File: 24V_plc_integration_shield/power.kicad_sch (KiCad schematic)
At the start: 9 parts, among them J2 USB_A_Stacked, J4 Screw_Terminal_01x02, J5 Conn_01x02_Female, U4 JTD2024S05

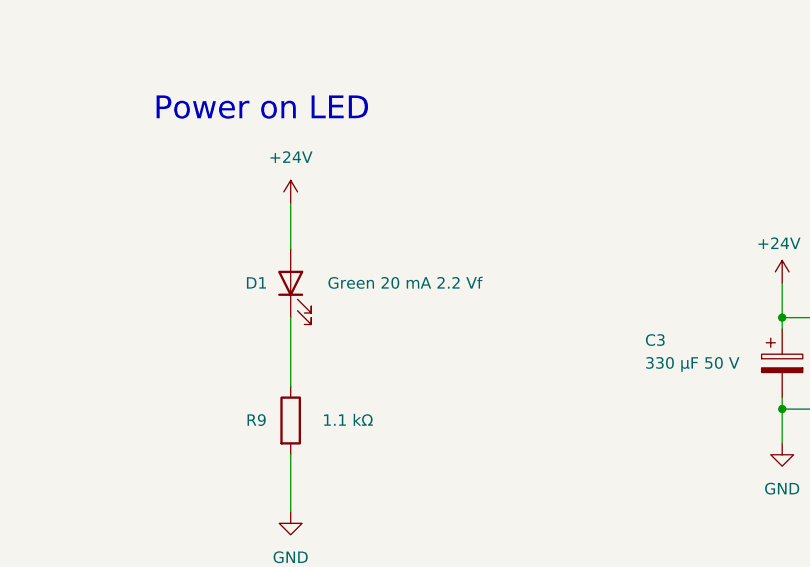
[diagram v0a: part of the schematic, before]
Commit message: added part details for smd led
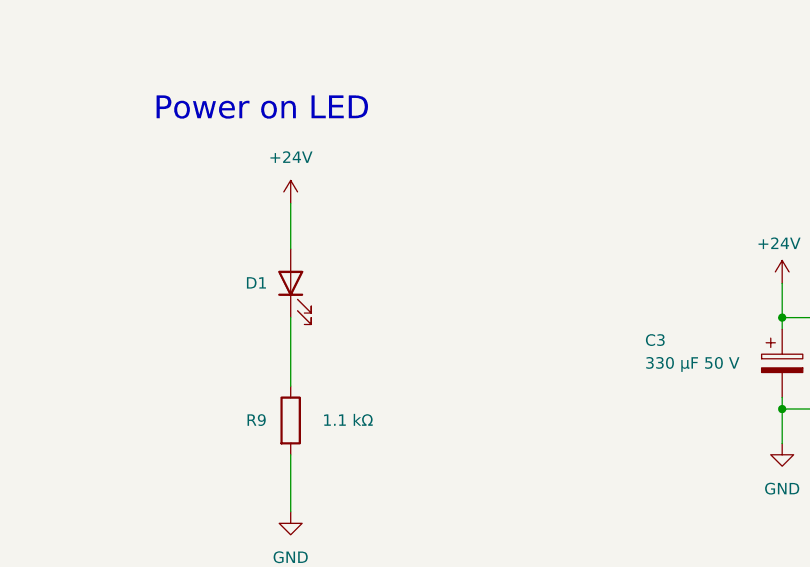
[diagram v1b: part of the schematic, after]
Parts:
- D1: value Green 20 mA 2.2 Vf -> (none); footprint LED_SMD:LED_0805_2012Metric_Pad1.15x1.40mm_HandSolder -> (none); MFP L-1503GD -> KPT-2012SGC; S1PL https://se.farnell.com/kingbright/l-1503gd/led-5mm-green-30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 -> https://se.farnell.com/kingbright/kpt-2012sgc/led-0805-gree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; S1PN 2335726 -> 2099239
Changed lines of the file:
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@@
     (in_bom yes) (on_board yes)
     (property "Reference" "D1" (id 0) (at 140.97 92.71 90))
-    (property "Value" "Green 20 mA 2.2 Vf" (id 1) (at 157.48 92.71 90))
-    (property "Footprint" "LED_SMD:LED_0805_2012Metric_Pad1.15x1.40mm_HandSolder" (id 2) (at 144.78 92.71 0)
+    (property "Value" "" (id 1) (at 157.48 92.71 90))
+    (property "Footprint" "" (id 2) (at 144.78 92.71 0)
       (effects (font (size 1.27 1.27)) hide)
     )
-    (property "Datasheet" "https://www.farnell.com/datasheets/2046482.pdf" (id 3) (at 144.78 92.71 0)
+    (property "Datasheet" "https://www.farnell.com/datasheets/2045828.pdf" (id 3) (at 144.78 92.71 0)
       (effects (font (size 1.27 1.27)) hide)
     )
-    (property "S1PL" "https://se.farnell.com/kingbright/l-1503gd/led-5mm-green-30mcd-568nm/dp/2335726" (id 4) (at 144.78 92.71 0)
+    (property "S1PL" "https://se.farnell.com/kingbright/kpt-2012sgc/led-0805-green-12mcd-568nm/dp/2099239" (id 4) (at 144.78 92.71 0)
       (effects (font (size 1.27 1.27)) hide)
     )
-    (property "S1PN" "2335726" (id 5) (at 144.78 92.71 0)
+    (property "S1PN" "2099239" (id 5) (at 144.78 92.71 0)
       (effects (font (size 1.27 1.27)) hide)
     )
@@
       (effects (font (size 1.27 1.27)) hide)
     )
-    (property "MFP" "L-1503GD" (id 7) (at 144.78 92.71 0)
+    (property "MFP" "KPT-2012SGC" (id 7) (at 144.78 92.71 0)
       (effects (font (size 1.27 1.27)) hide)
     )
